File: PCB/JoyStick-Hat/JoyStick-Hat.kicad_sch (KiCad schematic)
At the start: 0 parts

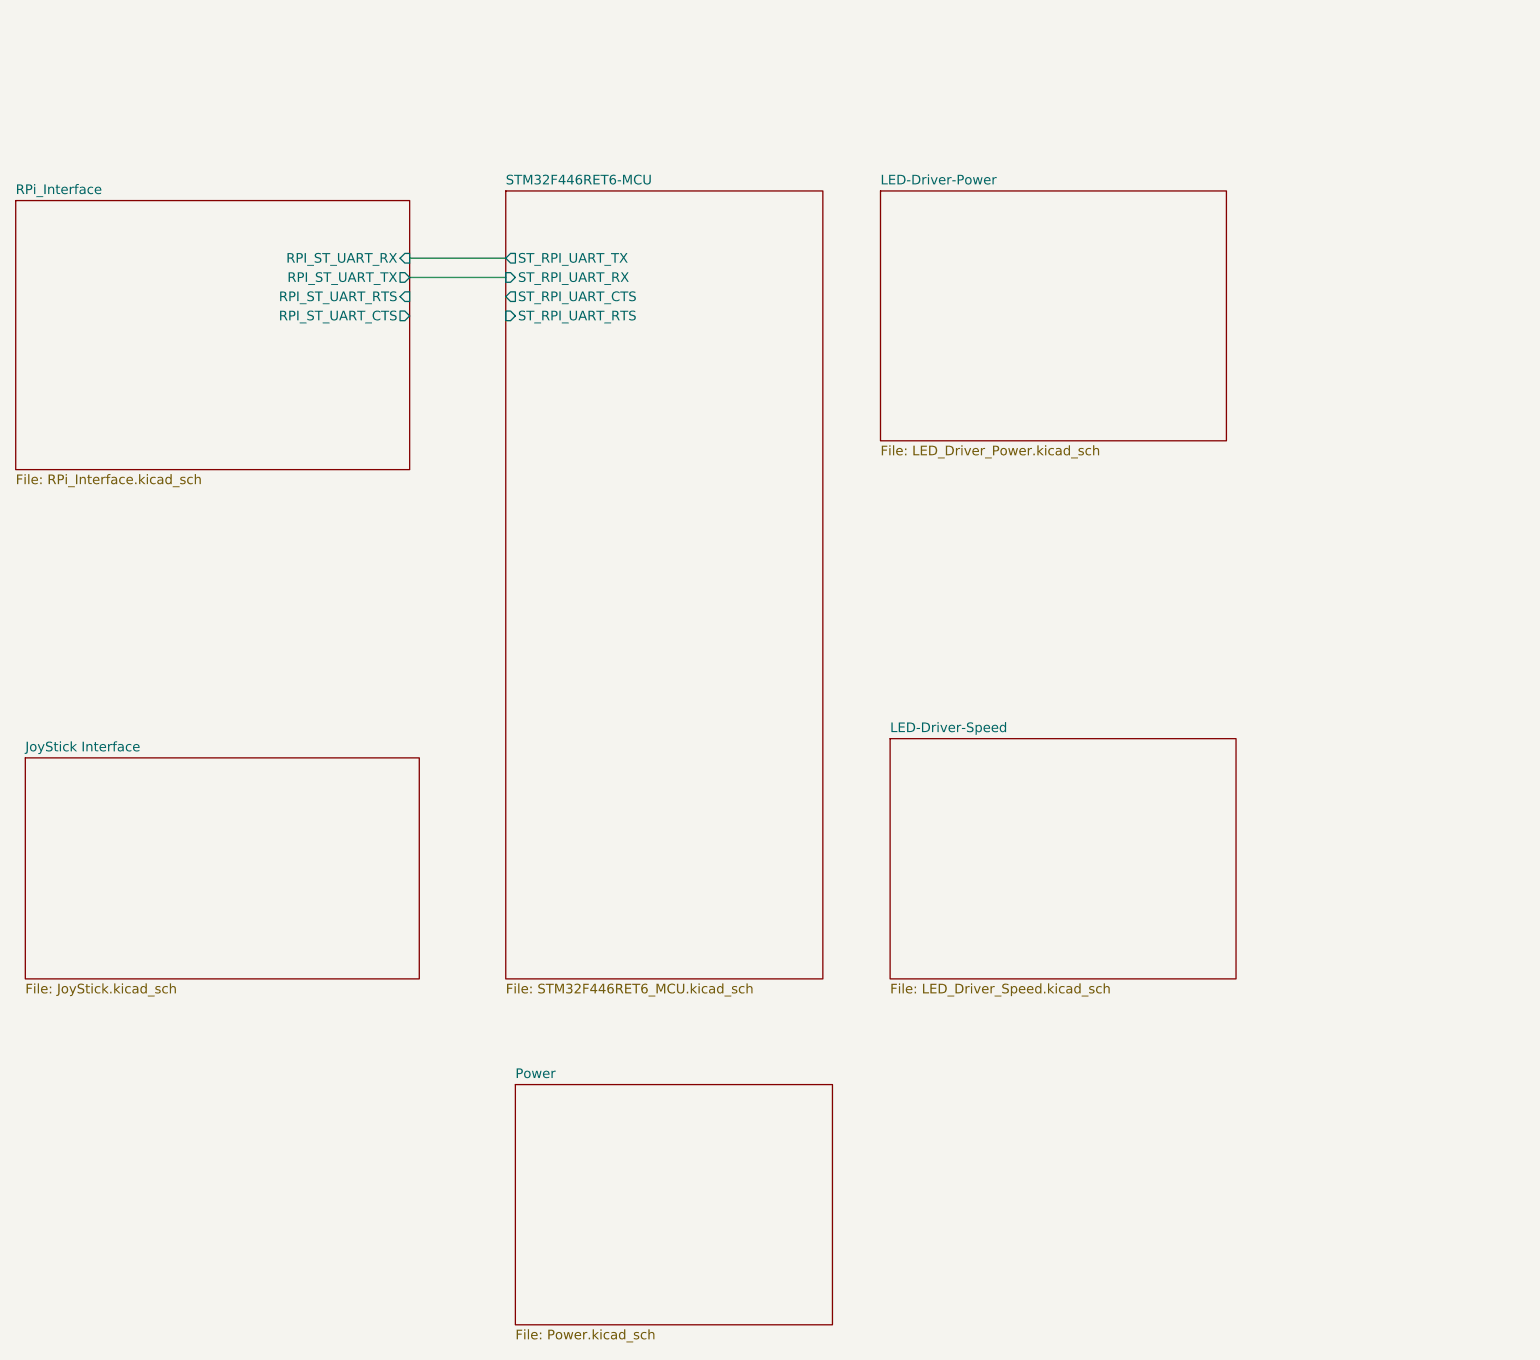
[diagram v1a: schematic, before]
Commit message: LED drivers and Joystick
Finished LED driver scheamtics, corrected some problems with symbols. added conenctors for joystick and buttons, connected RPI pins to MCU
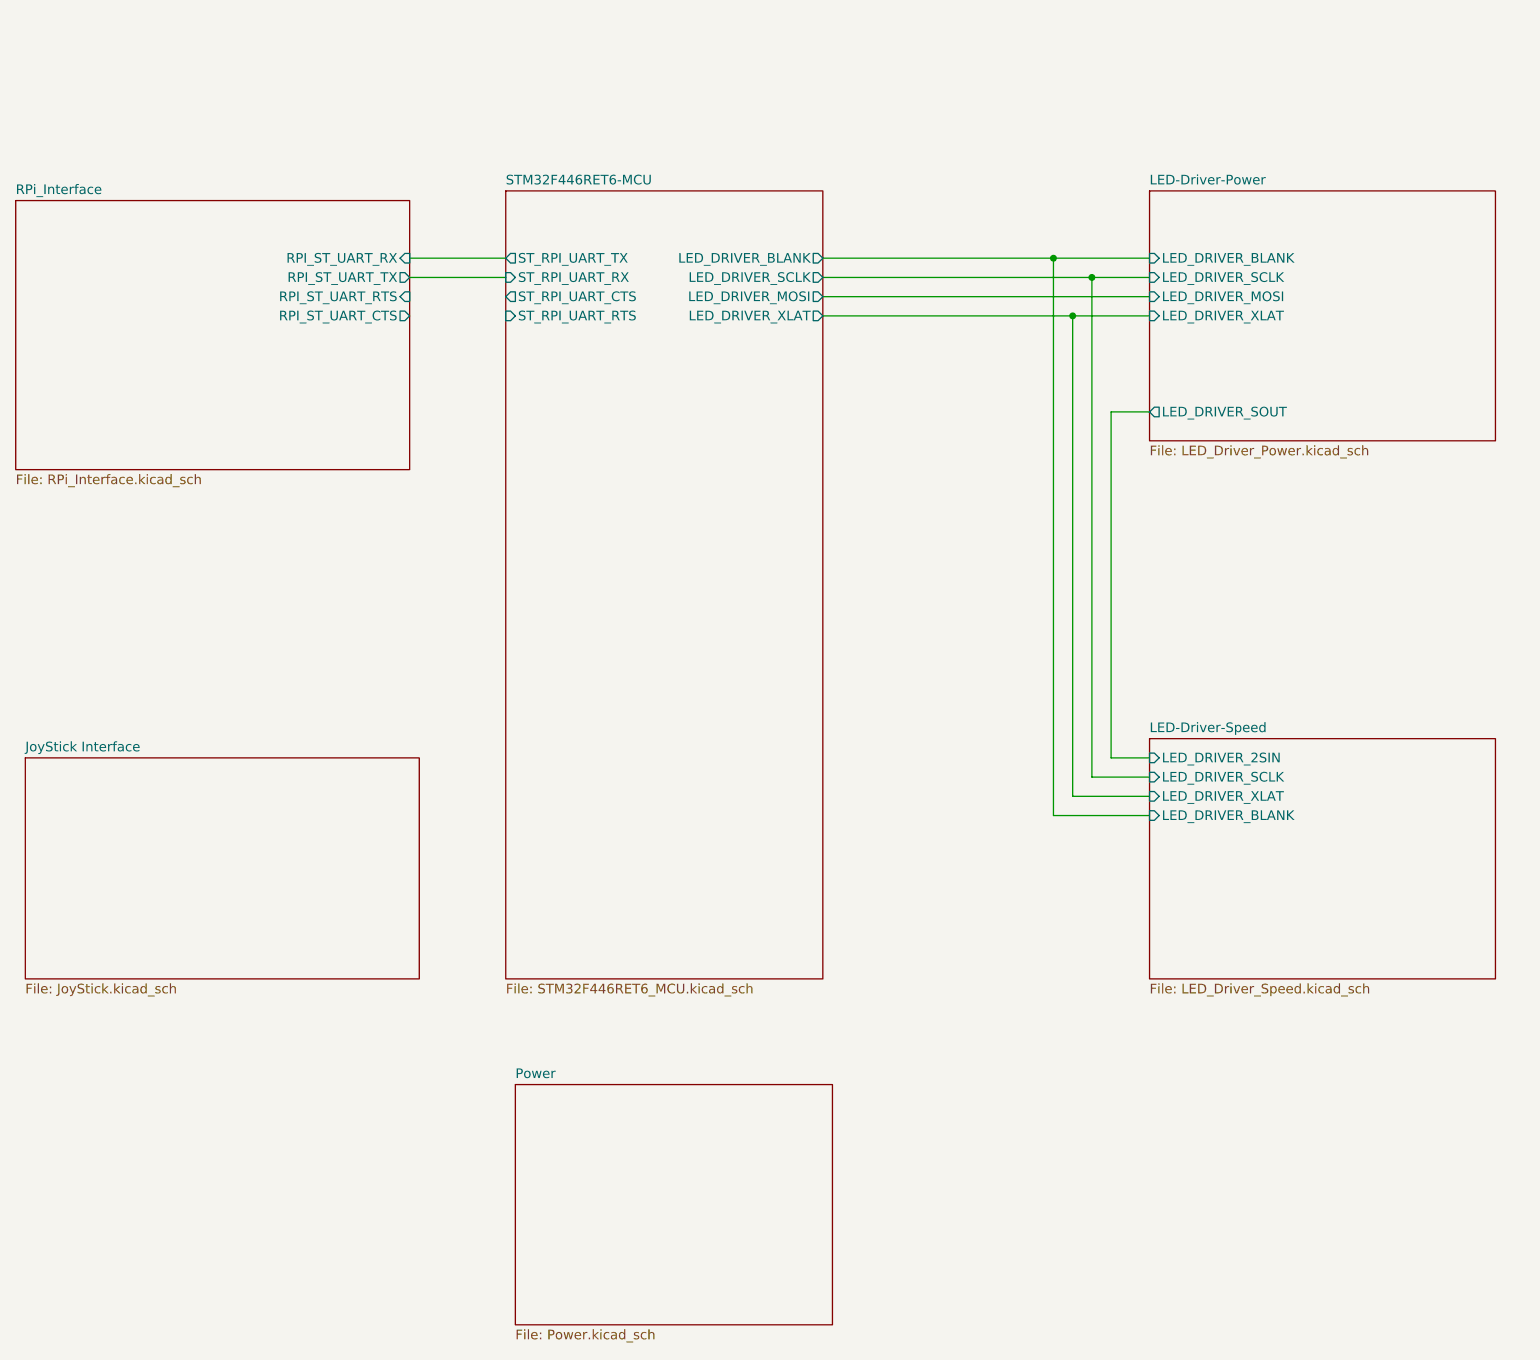
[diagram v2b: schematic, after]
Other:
- sheet LED-Driver-Power ports: added LED_DRIVER_BLANK, LED_DRIVER_MOSI, LED_DRIVER_SCLK, LED_DRIVER_SOUT, LED_DRIVER_XLAT; removed none
- sheet LED-Driver-Speed ports: added LED_DRIVER_2SIN, LED_DRIVER_BLANK, LED_DRIVER_SCLK, LED_DRIVER_XLAT; removed none
- sheet STM32F446RET6-MCU ports: added LED_DRIVER_BLANK, LED_DRIVER_MOSI, LED_DRIVER_SCLK, LED_DRIVER_XLAT; removed none
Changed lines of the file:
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@@
 (kicad_sch (version 20230121) (generator eeschema)
   (paper "A4")
+  (junction (at 185.42 50.8) (diameter 0) (color 0 0 0 0)
+  )
+  (junction (at 190.5 53.34) (diameter 0) (color 0 0 0 0)
+  )
+  (junction (at 187.96 58.42) (diameter 0) (color 0 0 0 0)
+  )
+  (wire (pts (xy 190.5 53.34) (xy 198.12 53.34))
+    (stroke (width 0) (type default))
+  )
+  (wire (pts (xy 187.96 58.42) (xy 187.96 121.92))
+    (stroke (width 0) (type default))
+  )
   (wire (pts (xy 100.33 53.34) (xy 113.03 53.34))
     (stroke (width 0) (type default))
   )
+  (wire (pts (xy 187.96 58.42) (xy 198.12 58.42))
+    (stroke (width 0) (type default))
+  )
+  (wire (pts (xy 193.04 71.12) (xy 198.12 71.12))
+    (stroke (width 0) (type default))
+  )
+  (wire (pts (xy 185.42 50.8) (xy 185.42 124.46))
+    (stroke (width 0) (type default))
+  )
+  (wire (pts (xy 154.94 58.42) (xy 187.96 58.42))
+    (stroke (width 0) (type default))
+  )
+  (wire (pts (xy 190.5 53.34) (xy 190.5 119.38))
+    (stroke (width 0) (type default))
+  )
+  (wire (pts (xy 187.96 121.92) (xy 198.12 121.92))
+    (stroke (width 0) (type default))
+  )
+  (wire (pts (xy 154.94 55.88) (xy 198.12 55.88))
+    (stroke (width 0) (type default))
+  )
+  (wire (pts (xy 190.5 119.38) (xy 198.12 119.38))
+    (stroke (width 0) (type default))
+  )
+  (wire (pts (xy 154.94 50.8) (xy 185.42 50.8))
+    (stroke (width 0) (type default))
+  )
+  (wire (pts (xy 185.42 50.8) (xy 198.12 50.8))
+    (stroke (width 0) (type default))
+  )
+  (wire (pts (xy 198.12 116.84) (xy 193.04 116.84))
+    (stroke (width 0) (type default))
+  )
+  (wire (pts (xy 193.04 116.84) (xy 193.04 71.12))
+    (stroke (width 0) (type default))
+  )
+  (wire (pts (xy 185.42 124.46) (xy 198.12 124.46))
+    (stroke (width 0) (type default))
+  )
   (wire (pts (xy 100.33 50.8) (xy 113.03 50.8))
     (stroke (width 0) (type default))
   )
-  (sheet (at 163.83 114.3) (size 45.72 31.75) (fields_autoplaced)
+  (wire (pts (xy 154.94 53.34) (xy 190.5 53.34))
+    (stroke (width 0) (type default))
+  )
+  (sheet (at 198.12 114.3) (size 45.72 31.75) (fields_autoplaced)
     (stroke (width 0.1524) (type solid))
     (fill (color 255 255 0 1.0000))
-    (property "Sheetname" "LED-Driver-Speed" (at 163.83 113.5884 0)
-      (effects (font (size 1.27 1.27)) (justify left bottom))
-    )
-    (property "Sheetfile" "LED_Driver_Speed.kicad_sch" (at 163.83 146.6346 0)
-      (effects (font (size 1.27 1.27)) (justify left top))
+    (property "Sheetname" "LED-Driver-Speed" (at 198.12 113.5884 0)
+      (effects (font (size 1.27 1.27)) (justify left bottom))
+    )
+    (property "Sheetfile" "LED_Driver_Speed.kicad_sch" (at 198.12 146.6346 0)
+      (effects (font (size 1.27 1.27)) (justify left top))
+    )
+    (pin "LED_DRIVER_XLAT" input (at 198.12 121.92 180)
+      (effects (font (size 1.27 1.27)) (justify left))
+    )
+    (pin "LED_DRIVER_SCLK" input (at 198.12 119.38 180)
+      (effects (font (size 1.27 1.27)) (justify left))
+    )
+    (pin "LED_DRIVER_BLANK" input (at 198.12 124.46 180)
+      (effects (font (size 1.27 1.27)) (justify left))
+    )
+    (pin "LED_DRIVER_2SIN" input (at 198.12 116.84 180)
+      (effects (font (size 1.27 1.27)) (justify left))
     )
     (instances
@@
     )
   )
-  (sheet (at 162.56 41.91) (size 45.72 33.02) (fields_autoplaced)
+  (sheet (at 198.12 41.91) (size 45.72 33.02) (fields_autoplaced)
     (stroke (width 0.1524) (type solid))
     (fill (color 255 255 0 1.0000))
-    (property "Sheetname" "LED-Driver-Power" (at 162.56 41.1984 0)
-      (effects (font (size 1.27 1.27)) (justify left bottom))
-    )
-    (property "Sheetfile" "LED_Driver_Power.kicad_sch" (at 162.56 75.5146 0)
-      (effects (font (size 1.27 1.27)) (justify left top))
+    (property "Sheetname" "LED-Driver-Power" (at 198.12 41.1984 0)
+      (effects (font (size 1.27 1.27)) (justify left bottom))
+    )
+    (property "Sheetfile" "LED_Driver_Power.kicad_sch" (at 198.12 75.5146 0)
+      (effects (font (size 1.27 1.27)) (justify left top))
+    )
+    (pin "LED_DRIVER_SOUT" output (at 198.12 71.12 180)
+      (effects (font (size 1.27 1.27)) (justify left))
+    )
+    (pin "LED_DRIVER_SCLK" input (at 198.12 53.34 180)
+      (effects (font (size 1.27 1.27)) (justify left))
+    )
+    (pin "LED_DRIVER_MOSI" input (at 198.12 55.88 180)
+      (effects (font (size 1.27 1.27)) (justify left))
+    )
+    (pin "LED_DRIVER_XLAT" input (at 198.12 58.42 180)
+      (effects (font (size 1.27 1.27)) (justify left))
+    )
+    (pin "LED_DRIVER_BLANK" input (at 198.12 50.8 180)
+      (effects (font (size 1.27 1.27)) (justify left))
     )
     (instances
@@
       (effects (font (size 1.27 1.27)) (justify left))
     )
-    (instances
+    (pin "LED_DRIVER_BLANK" output (at 154.94 50.8 0)
+      (effects (font (size 1.27 1.27)) (justify right))
+    )
+    (pin "LED_DRIVER_SCLK" output (at 154.94 53.34 0)
+      (effects (font (size 1.27 1.27)) (justify right))
+    )
+    (pin "LED_DRIVER_MOSI" output (at 154.94 55.88 0)
+      (effects (font (size 1.27 1.27)) (justify right))
+    )
+    (pin "LED_DRIVER_XLAT" output (at 154.94 58.42 0)
+      (effects (font (size 1.27 1.27)) (justify right))
+    )
+    (instances
